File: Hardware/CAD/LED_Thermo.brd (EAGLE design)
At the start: 54.9 x 55 mm, 44 parts, among them IC1 MEGA68-AU, IC2 MAX481CSA, IC3 IP4220CZ6, Q1 12MHZ, SW1 B3FS-1002

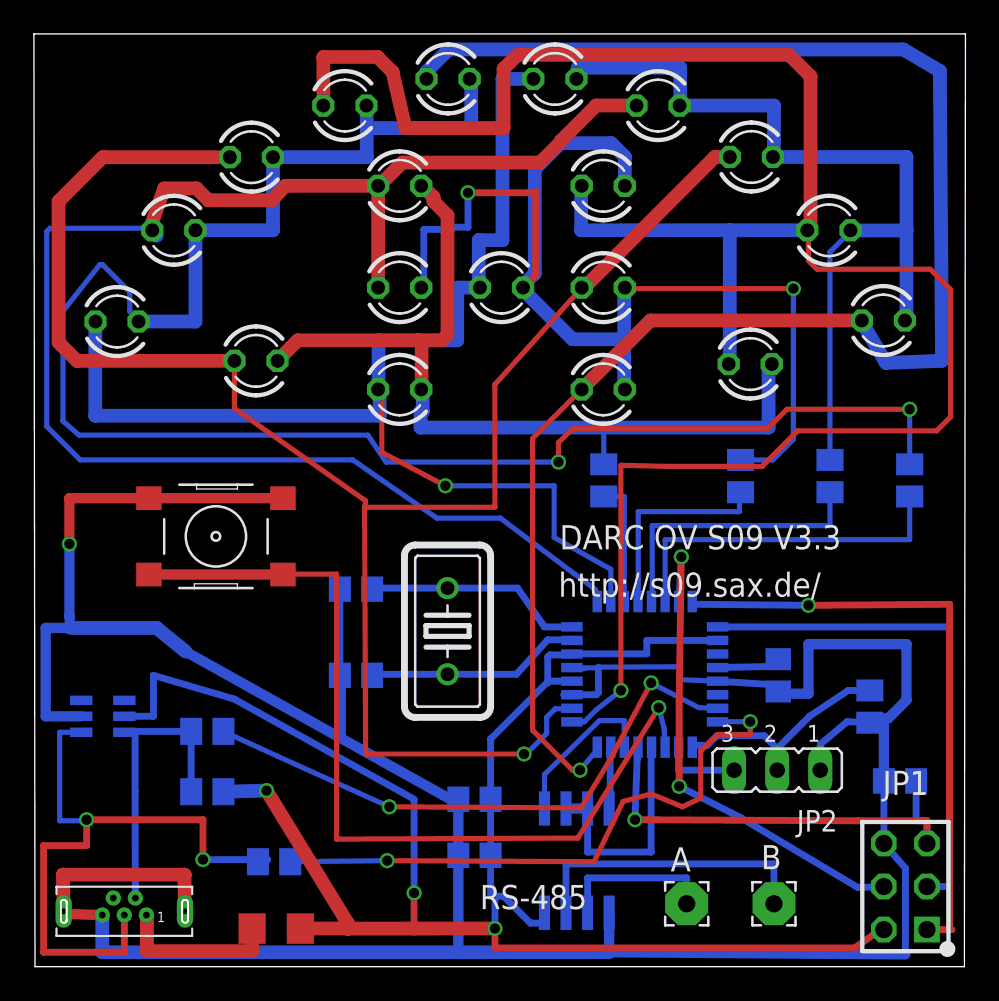
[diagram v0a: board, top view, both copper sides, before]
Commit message: c und h Files ueberarbeitet, dabei Fehler in Schaltplan gefunden, diesen beseitigt aber keine neuen Gerberdateien erzeugt
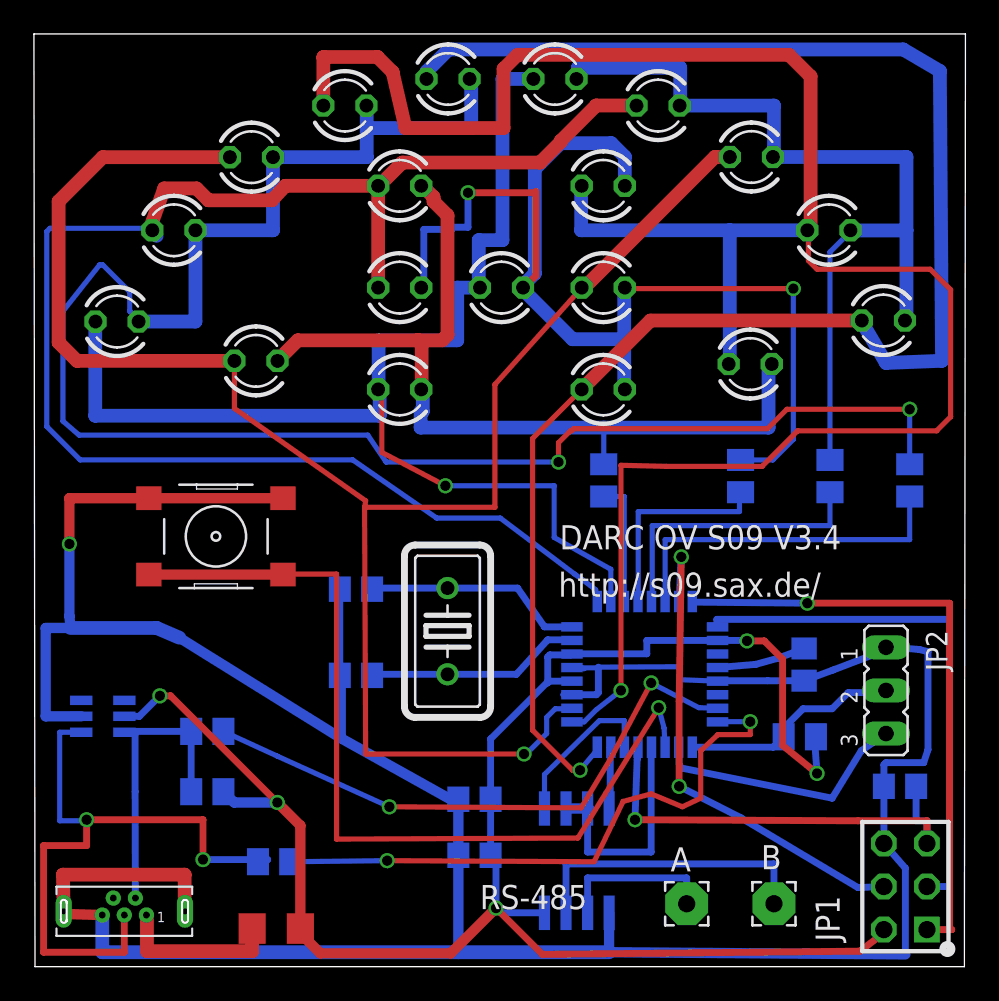
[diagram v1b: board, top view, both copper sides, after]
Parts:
- moved JP2 7.95 mm to (50.2, 16.3), turned to 270 degrees
- moved R11 4.49 mm to (45.1, 13.5), turned to 0 degrees
- moved C7 1.65 mm to (45.3, 17.8)
- moved C8 0.32 mm to (51.0, 10.6)
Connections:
- net GND: no longer R11.1
- net VCC: now also R11.1
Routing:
- net N$31: track 4.62 -> 15.4 mm
- net GND: track 194.1 -> 186.3 mm
- net VCC: track 112.8 -> 109.1 mm, vias 3 -> 5
- net N$20: track 3.83 -> 5.26 mm
- net N$15: track 30.4 -> 31.3 mm
- net N$33: track 13.7 -> 13.1 mm
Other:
- board text added: "DARC OV S09 V3.4"
- board text removed: "DARC OV S09 V3.3"
